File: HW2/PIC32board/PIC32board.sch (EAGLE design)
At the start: 24 parts

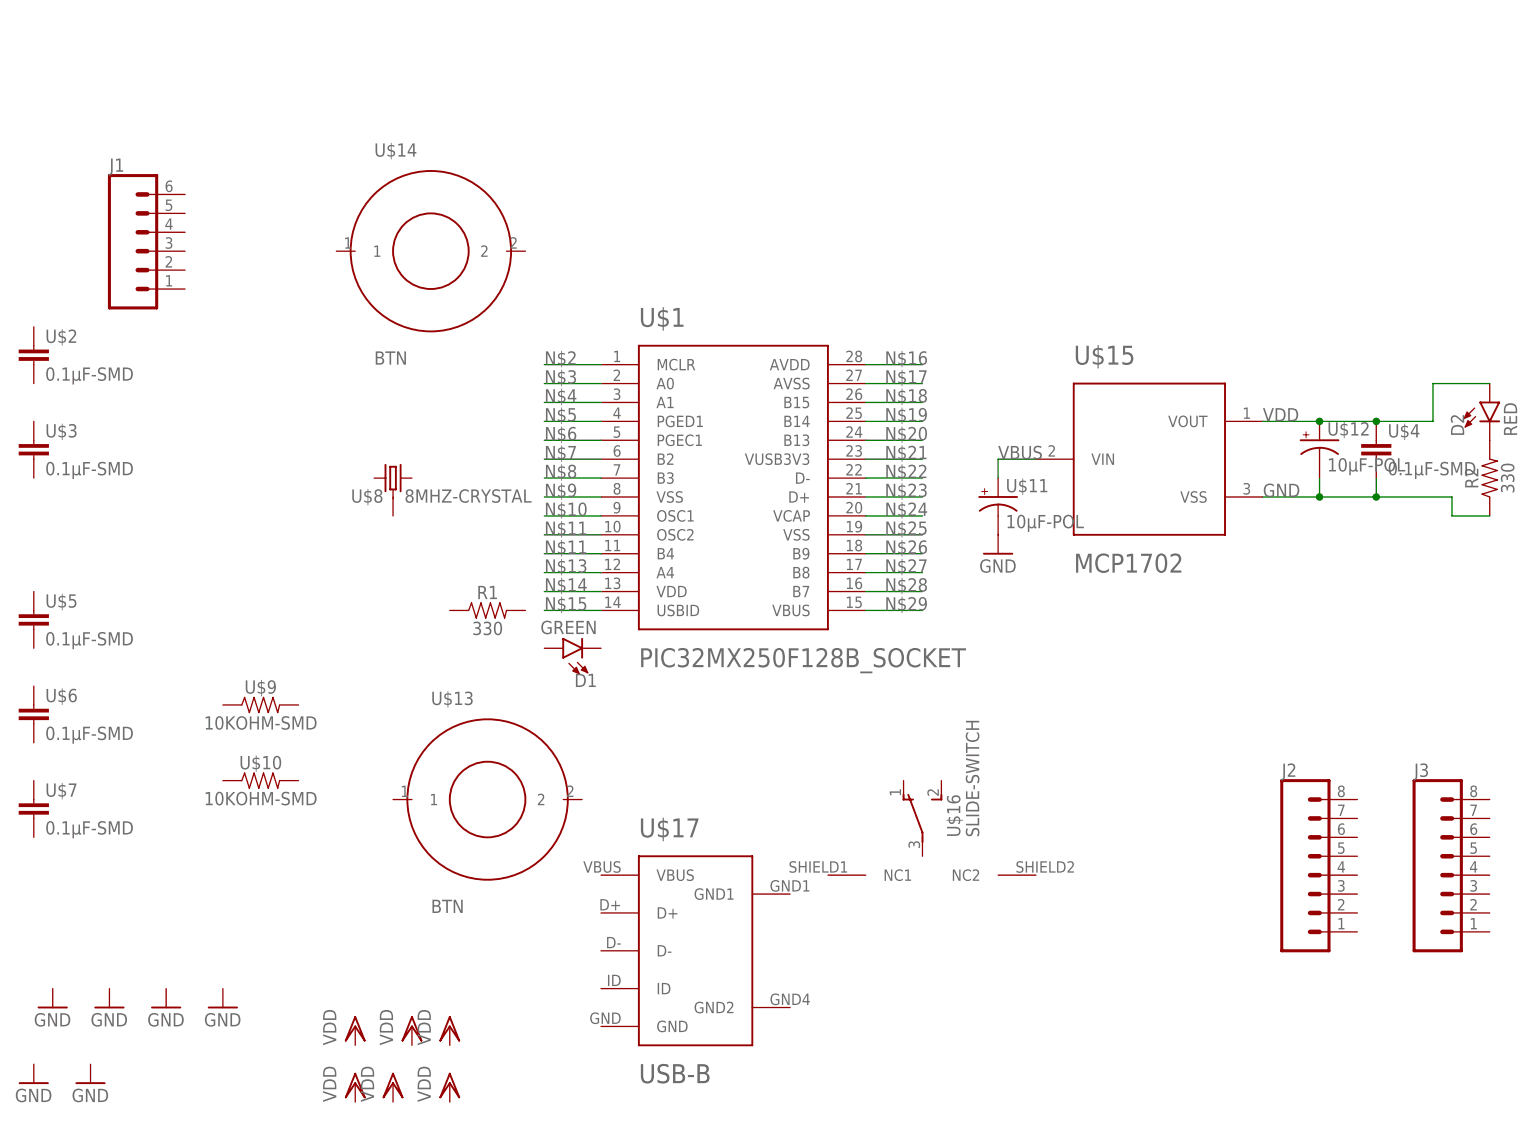
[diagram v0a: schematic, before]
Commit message: finished first draft of schematic
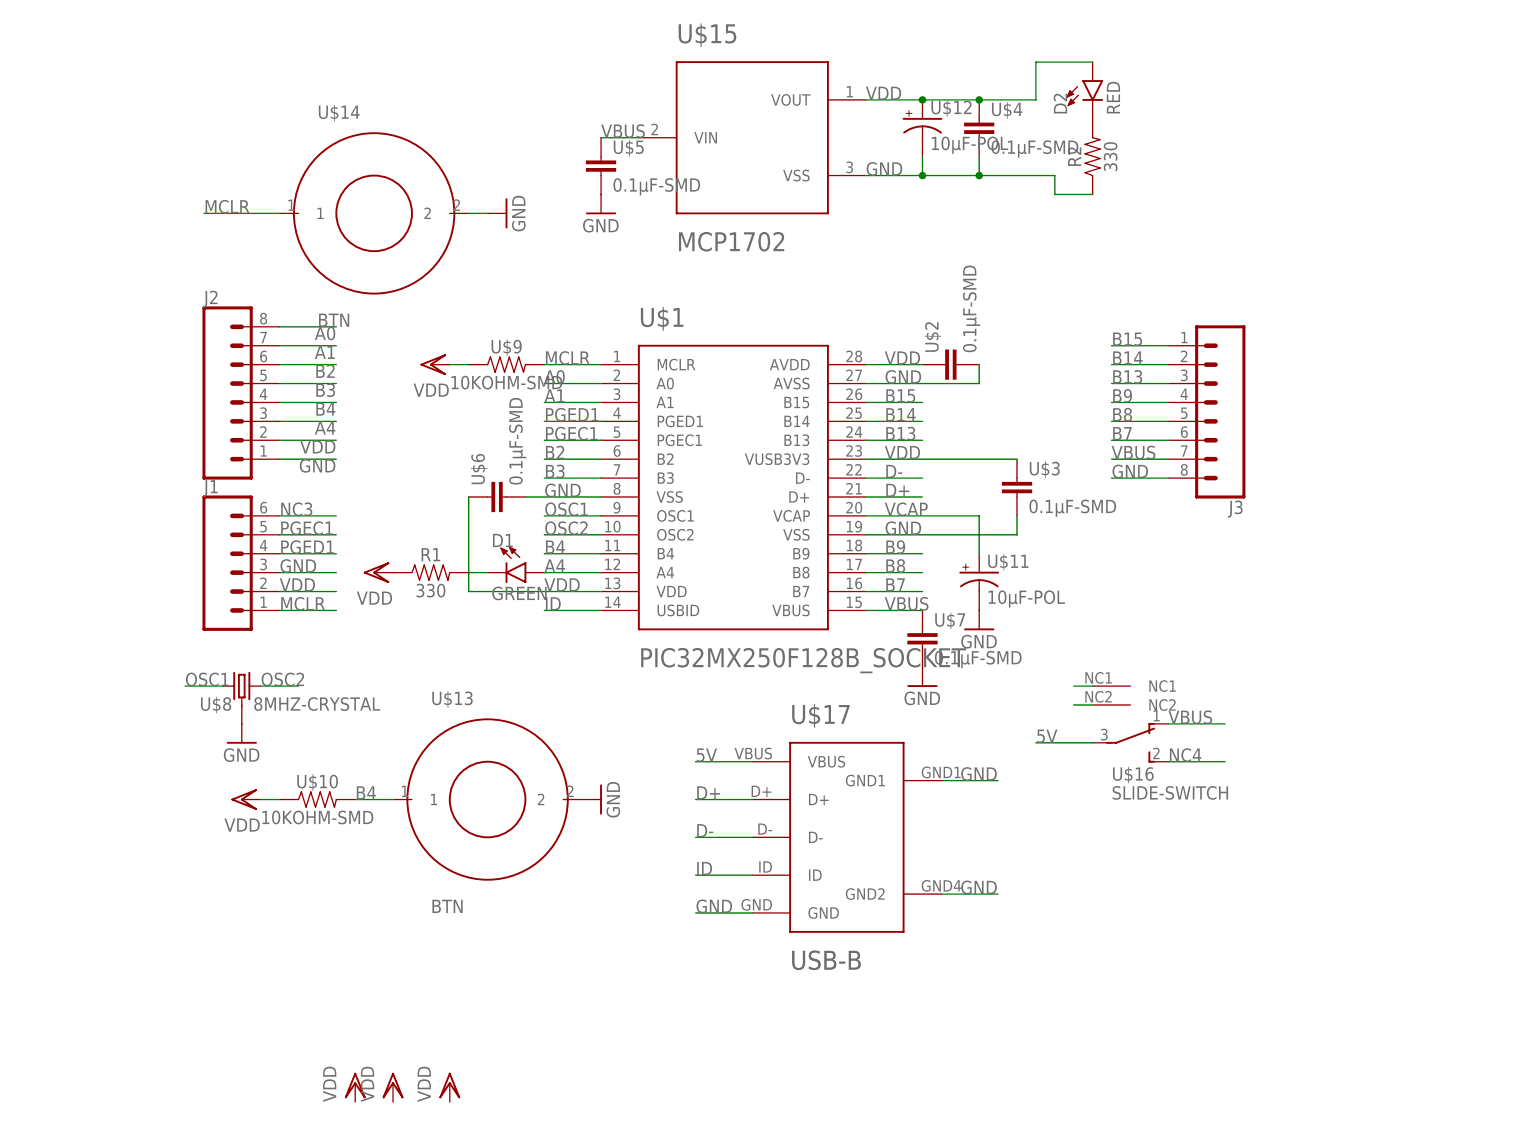
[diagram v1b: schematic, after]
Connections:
- removed net N$10: U$1.OSC1
- removed net N$11: U$1.OSC2
- removed net N$12: U$1.B4
- removed net N$13: U$1.A4
- removed net N$14: U$1.VDD
- removed net N$15: U$1.USBID
- removed net N$16: U$1.AVDD
- removed net N$17: U$1.AVSS
- removed net N$18: U$1.B15
- removed net N$19: U$1.B14
- removed net N$20: U$1.B13
- removed net N$21: U$1.VUSB3V3
- removed net N$22: U$1.D-
- removed net N$23: U$1.D+
- removed net N$24: U$1.VCAP
- removed net N$25: U$1.VSS@19
- removed net N$26: U$1.B9
- removed net N$27: U$1.B8
- removed net N$28: U$1.B7
- removed net N$29: U$1.VBUS
- removed net N$3: U$1.A0
- removed net N$4: U$1.A1
- removed net N$5: U$1.PGED1
- removed net N$6: U$1.PGEC1
- removed net N$7: U$1.B2
- removed net N$8: U$1.B3
- removed net N$9: U$1.VSS@8
- new net 5V: U$16.3, U$17.VBUS
- new net A0: J2.8, U$1.A0
- new net A1: J2.7, U$1.A1
- new net A4: D1.A, J2.3, U$1.A4
- new net B13: J3.3, U$1.B13
- new net B14: J3.2, U$1.B14
- new net B15: J3.1, U$1.B15
- new net B2: J2.6, U$1.B2
- new net B3: J2.5, U$1.B3
- new net B4: J2.4, U$1.B4, U$10.2, U$13.1
- new net B7: J3.6, U$1.B7
- new net B8: J3.5, U$1.B8
- new net B9: J3.4, U$1.B9
- new net D+: U$1.D+, U$17.D+
- new net D-: U$1.D-, U$17.D-
- new net ID: U$1.USBID, U$17.ID
- new net MCLR: J1.1, U$1.MCLR, U$14.1, U$9.2
- new net NC1: U$16.NC1
- new net NC2: U$16.NC2
- new net NC3: J1.6
- new net NC4: U$16.2
- new net OSC1: U$1.OSC1, U$8.1
- new net OSC2: U$1.OSC2, U$8.2
- new net PGEC1: J1.5, U$1.PGEC1
- new net PGED1: J1.4, U$1.PGED1
- new net VCAP: U$1.VCAP, U$11.+
- net GND: now also J1.3, J2.1, J3.8, U$1.AVSS, U$1.VSS@19, U$1.VSS@8, U$13.2, U$14.2, U$17.GND, U$17.GND1, U$17.GND2, U$2.2, U$3.2, U$5.2, U$6.2, U$7.2, U$8.VSS
- net N$2: now also D1.C, R1.2; no longer U$1.MCLR
- net VBUS: now also J3.7, U$1.VBUS, U$16.1, U$5.1, U$7.1; no longer U$11.+
- net VDD: now also J1.2, J2.2, R1.1, U$1.AVDD, U$1.VDD, U$1.VUSB3V3, U$10.1, U$2.1, U$3.1, U$6.1, U$9.1
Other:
- moved on the sheet: D1, D2, J1, J2, J3, R1, R2, U$10, U$11, U$12, U$14, U$15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
